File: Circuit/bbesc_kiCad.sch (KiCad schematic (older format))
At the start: 79 parts, among them J1 CONN_01X02, J10 CONN_01X01, J11 CONN_01X01, J12 CONN_01X01, J13 CONN_01X01, J14 CONN_01X01, J15 CONN_01X02, J16 CONN_01X02, J17 CONN_01X01, J18 CONN_01X01, J19 CONN_01X01, J2 CONN_01X06, J3 CONN_01X06, J4 CONN_01X06, J5 CONN_01X02, J6 CONN_01X02, J7 CONN_01X01, J8 CONN_01X01, J9 RJ45, Q1 Q_NMOS_GDS, Q2 Q_NMOS_GDS, Q3 Q_NMOS_GDS, Q4 Q_NMOS_GDS, Q5 Q_NMOS_GDS, Q6 Q_NMOS_GDS, U1 teensy_3-2, U2 IR2101, U3 IR2101, U4 IR2101, U5 LM324N, U6 LM7805

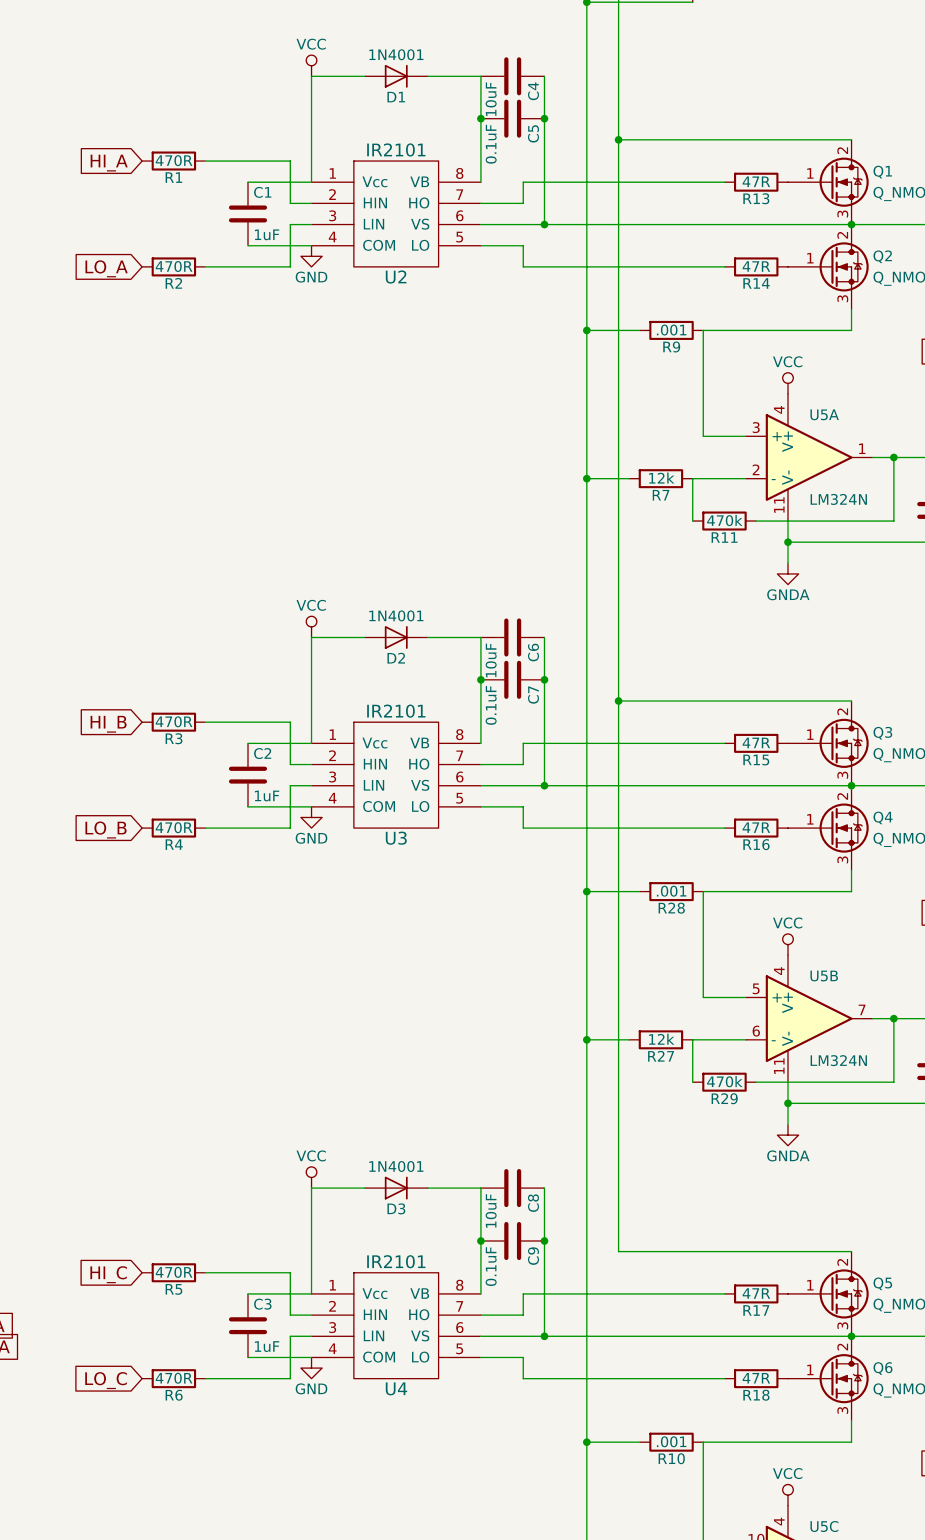
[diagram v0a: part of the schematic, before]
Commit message: smaller R on drivers
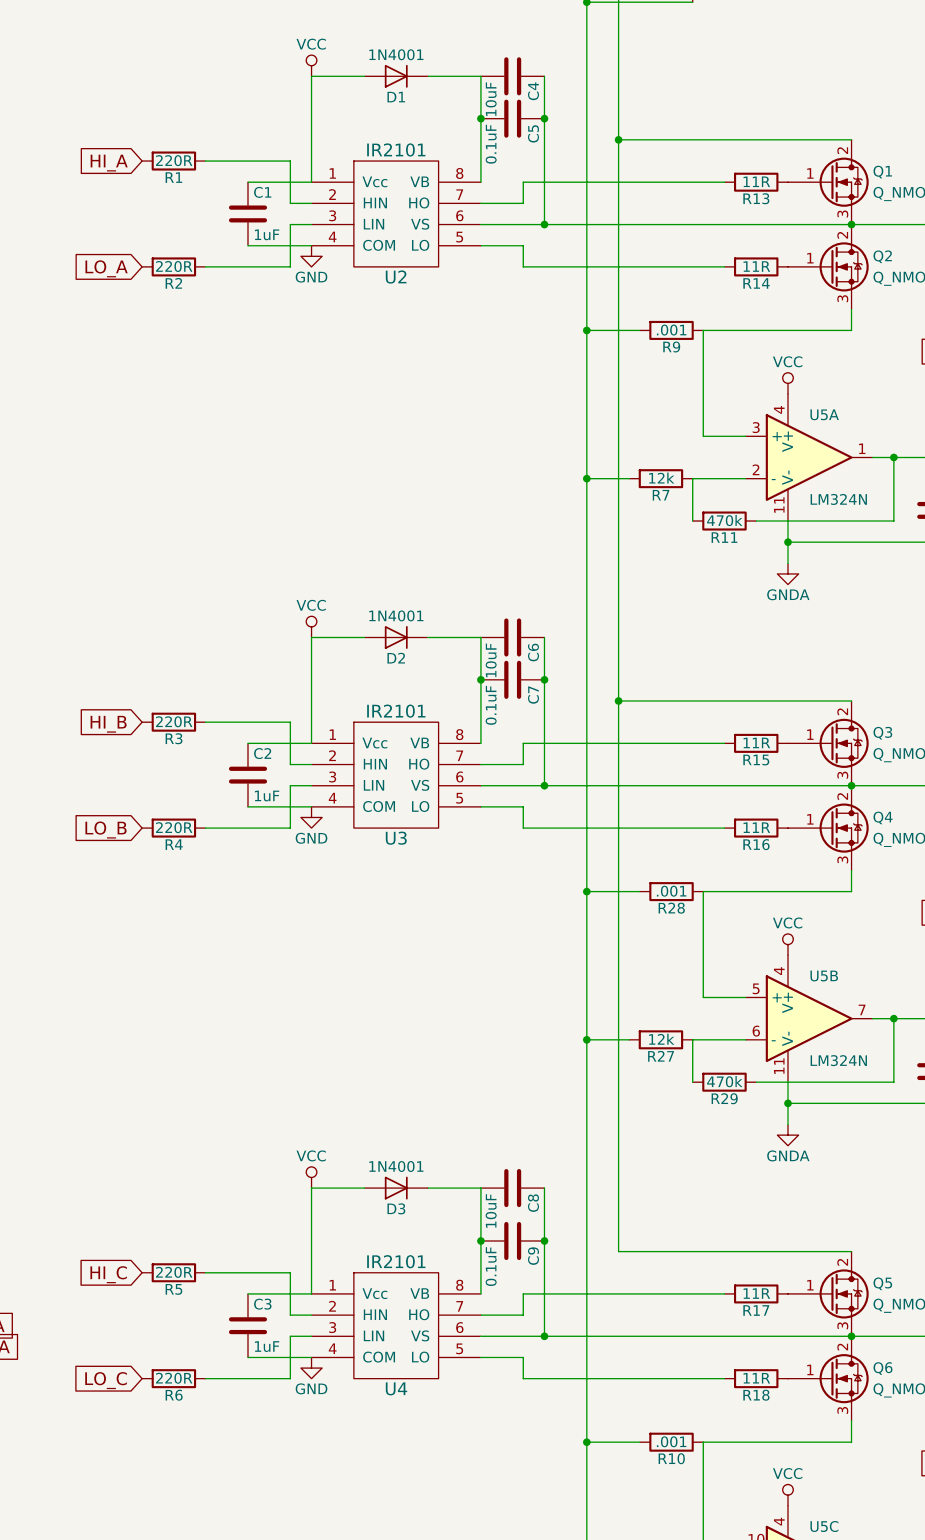
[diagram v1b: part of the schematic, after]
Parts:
- R1, R2, R3, R4, R5, R6: value 470R -> 220R
- R13, R14, R15, R16, R17, R18: value 47R -> 11R
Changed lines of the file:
@@
 LIBS:valves
 LIBS:ir2101_kiCadComponent
-LIBS:smd-compLib
 LIBS:teensy_3-2_kiCadComponent
-LIBS:SMD-pcb-v03-r01-cache
 LIBS:bbesc_kiCad-cache
 EELAYER 25 0
@@
 P 10450 7450
 F 0 "R17" V 10530 7450 50  0000 C CNN
-F 1 "47R" V 10450 7450 50  0000 C CNN
+F 1 "11R" V 10450 7450 50  0000 C CNN
 F 2 "Resistors_SMD:R_1206_HandSoldering" V 10380 7450 50  0001 C CNN
 F 3 "" H 10450 7450 50  0001 C CNN
@@
 P 10450 7850
 F 0 "R18" V 10530 7850 50  0000 C CNN
-F 1 "47R" V 10450 7850 50  0000 C CNN
+F 1 "11R" V 10450 7850 50  0000 C CNN
 F 2 "Resistors_SMD:R_1206_HandSoldering" V 10380 7850 50  0001 C CNN
 F 3 "" H 10450 7850 50  0001 C CNN
@@
 P 7700 7350
 F 0 "R5" V 7780 7350 50  0000 C CNN
-F 1 "470R" V 7700 7350 50  0000 C CNN
+F 1 "220R" V 7700 7350 50  0000 C CNN
 F 2 "Resistors_SMD:R_1206_HandSoldering" V 7630 7350 50  0001 C CNN
 F 3 "" H 7700 7350 50  0001 C CNN
@@
 P 7700 7850
 F 0 "R6" V 7780 7850 50  0000 C CNN
-F 1 "470R" V 7700 7850 50  0000 C CNN
+F 1 "220R" V 7700 7850 50  0000 C CNN
 F 2 "Resistors_SMD:R_1206_HandSoldering" V 7630 7850 50  0001 C CNN
 F 3 "" H 7700 7850 50  0001 C CNN
@@
 P 10450 4850
 F 0 "R15" V 10530 4850 50  0000 C CNN
-F 1 "47R" V 10450 4850 50  0000 C CNN
+F 1 "11R" V 10450 4850 50  0000 C CNN
 F 2 "Resistors_SMD:R_1206_HandSoldering" V 10380 4850 50  0001 C CNN
 F 3 "" H 10450 4850 50  0001 C CNN
@@
 P 10450 5250
 F 0 "R16" V 10530 5250 50  0000 C CNN
-F 1 "47R" V 10450 5250 50  0000 C CNN
+F 1 "11R" V 10450 5250 50  0000 C CNN
 F 2 "Resistors_SMD:R_1206_HandSoldering" V 10380 5250 50  0001 C CNN
 F 3 "" H 10450 5250 50  0001 C CNN
@@
 P 7700 4750
 F 0 "R3" V 7780 4750 50  0000 C CNN
-F 1 "470R" V 7700 4750 50  0000 C CNN
+F 1 "220R" V 7700 4750 50  0000 C CNN
 F 2 "Resistors_SMD:R_1206_HandSoldering" V 7630 4750 50  0001 C CNN
 F 3 "" H 7700 4750 50  0001 C CNN
@@
 P 7700 5250
 F 0 "R4" V 7780 5250 50  0000 C CNN
-F 1 "470R" V 7700 5250 50  0000 C CNN
+F 1 "220R" V 7700 5250 50  0000 C CNN
 F 2 "Resistors_SMD:R_1206_HandSoldering" V 7630 5250 50  0001 C CNN
 F 3 "" H 7700 5250 50  0001 C CNN
@@
 P 10450 2200
 F 0 "R13" V 10530 2200 50  0000 C CNN
-F 1 "47R" V 10450 2200 50  0000 C CNN
+F 1 "11R" V 10450 2200 50  0000 C CNN
 F 2 "Resistors_SMD:R_1206_HandSoldering" V 10380 2200 50  0001 C CNN
 F 3 "" H 10450 2200 50  0001 C CNN
@@
 P 10450 2600
 F 0 "R14" V 10530 2600 50  0000 C CNN
-F 1 "47R" V 10450 2600 50  0000 C CNN
+F 1 "11R" V 10450 2600 50  0000 C CNN
 F 2 "Resistors_SMD:R_1206_HandSoldering" V 10380 2600 50  0001 C CNN
 F 3 "" H 10450 2600 50  0001 C CNN
@@
 P 7700 2100
 F 0 "R1" V 7780 2100 50  0000 C CNN
-F 1 "470R" V 7700 2100 50  0000 C CNN
+F 1 "220R" V 7700 2100 50  0000 C CNN
 F 2 "Resistors_SMD:R_1206_HandSoldering" V 7630 2100 50  0001 C CNN
 F 3 "" H 7700 2100 50  0001 C CNN
@@
 P 7700 2600
 F 0 "R2" V 7780 2600 50  0000 C CNN
-F 1 "470R" V 7700 2600 50  0000 C CNN
+F 1 "220R" V 7700 2600 50  0000 C CNN
 F 2 "Resistors_SMD:R_1206_HandSoldering" V 7630 2600 50  0001 C CNN
 F 3 "" H 7700 2600 50  0001 C CNN

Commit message: mv to linux
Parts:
- D4, D5: symbol LED -> LED-RESCUE-bbesc_kiCad
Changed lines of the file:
@@
 $EndComp
 $Comp
-L LED D5
+L LED-RESCUE-bbesc_kiCad D5
 U 1 1 591AB647
 P 5800 8400
@@
 $EndComp
 $Comp
-L LED D4
+L LED-RESCUE-bbesc_kiCad D4
 U 1 1 591B0D3D
 P 3500 7700

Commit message: minors
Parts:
- C1, C2, C3: value 1uF -> 47uF
- R13, R14, R15, R16, R17, R18: value 11R -> 4R7
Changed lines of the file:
@@
 P 10450 7450
 F 0 "R17" V 10530 7450 50  0000 C CNN
-F 1 "11R" V 10450 7450 50  0000 C CNN
+F 1 "4R7" V 10450 7450 50  0000 C CNN
 F 2 "Resistors_SMD:R_1206_HandSoldering" V 10380 7450 50  0001 C CNN
 F 3 "" H 10450 7450 50  0001 C CNN
@@
 P 10450 7850
 F 0 "R18" V 10530 7850 50  0000 C CNN
-F 1 "11R" V 10450 7850 50  0000 C CNN
+F 1 "4R7" V 10450 7850 50  0000 C CNN
 F 2 "Resistors_SMD:R_1206_HandSoldering" V 10380 7850 50  0001 C CNN
 F 3 "" H 10450 7850 50  0001 C CNN
@@
 P 8050 7600
 F 0 "C3" H 8075 7700 50  0000 L CNN
-F 1 "1uF" H 8075 7500 50  0000 L CNN
+F 1 "47uF" H 8075 7500 50  0000 L CNN
 F 2 "Capacitors_SMD:C_1206_HandSoldering" H 8088 7450 50  0001 C CNN
 F 3 "" H 8050 7600 50  0001 C CNN
@@
 P 10450 4850
 F 0 "R15" V 10530 4850 50  0000 C CNN
-F 1 "11R" V 10450 4850 50  0000 C CNN
+F 1 "4R7" V 10450 4850 50  0000 C CNN
 F 2 "Resistors_SMD:R_1206_HandSoldering" V 10380 4850 50  0001 C CNN
 F 3 "" H 10450 4850 50  0001 C CNN
@@
 P 10450 5250
 F 0 "R16" V 10530 5250 50  0000 C CNN
-F 1 "11R" V 10450 5250 50  0000 C CNN
+F 1 "4R7" V 10450 5250 50  0000 C CNN
 F 2 "Resistors_SMD:R_1206_HandSoldering" V 10380 5250 50  0001 C CNN
 F 3 "" H 10450 5250 50  0001 C CNN
@@
 P 8050 5000
 F 0 "C2" H 8075 5100 50  0000 L CNN
-F 1 "1uF" H 8075 4900 50  0000 L CNN
+F 1 "47uF" H 8075 4900 50  0000 L CNN
 F 2 "Capacitors_SMD:C_1206_HandSoldering" H 8088 4850 50  0001 C CNN
 F 3 "" H 8050 5000 50  0001 C CNN
@@
 P 10450 2200
 F 0 "R13" V 10530 2200 50  0000 C CNN
-F 1 "11R" V 10450 2200 50  0000 C CNN
+F 1 "4R7" V 10450 2200 50  0000 C CNN
 F 2 "Resistors_SMD:R_1206_HandSoldering" V 10380 2200 50  0001 C CNN
 F 3 "" H 10450 2200 50  0001 C CNN
@@
 P 10450 2600
 F 0 "R14" V 10530 2600 50  0000 C CNN
-F 1 "11R" V 10450 2600 50  0000 C CNN
+F 1 "4R7" V 10450 2600 50  0000 C CNN
 F 2 "Resistors_SMD:R_1206_HandSoldering" V 10380 2600 50  0001 C CNN
 F 3 "" H 10450 2600 50  0001 C CNN
@@
 P 8050 2350
 F 0 "C1" H 8075 2450 50  0000 L CNN
-F 1 "1uF" H 8075 2250 50  0000 L CNN
+F 1 "47uF" H 8075 2250 50  0000 L CNN
 F 2 "Capacitors_SMD:C_1206_HandSoldering" H 8088 2200 50  0001 C CNN
 F 3 "" H 8050 2350 50  0001 C CNN
